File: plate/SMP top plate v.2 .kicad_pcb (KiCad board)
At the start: 2 copper layers, 123.8 x 58.7 mm, 4 parts

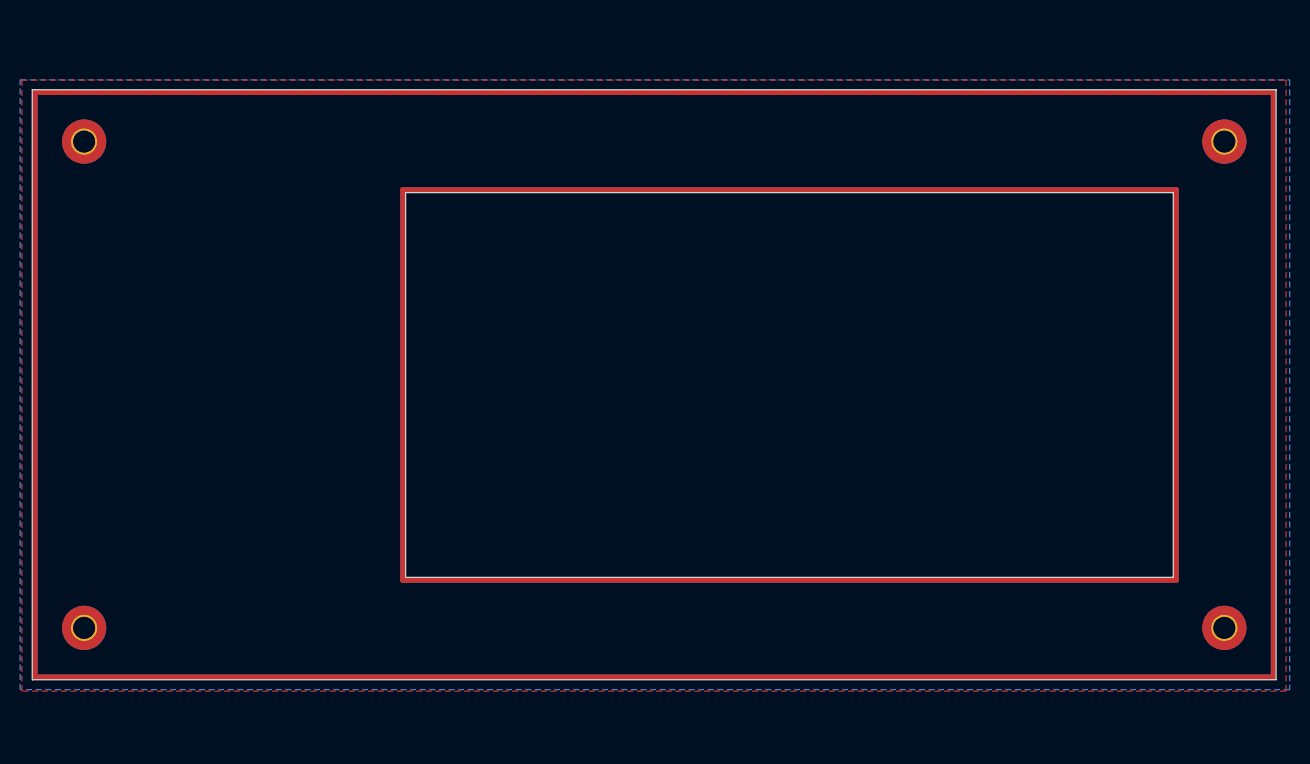
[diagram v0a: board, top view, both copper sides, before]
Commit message: update top plate
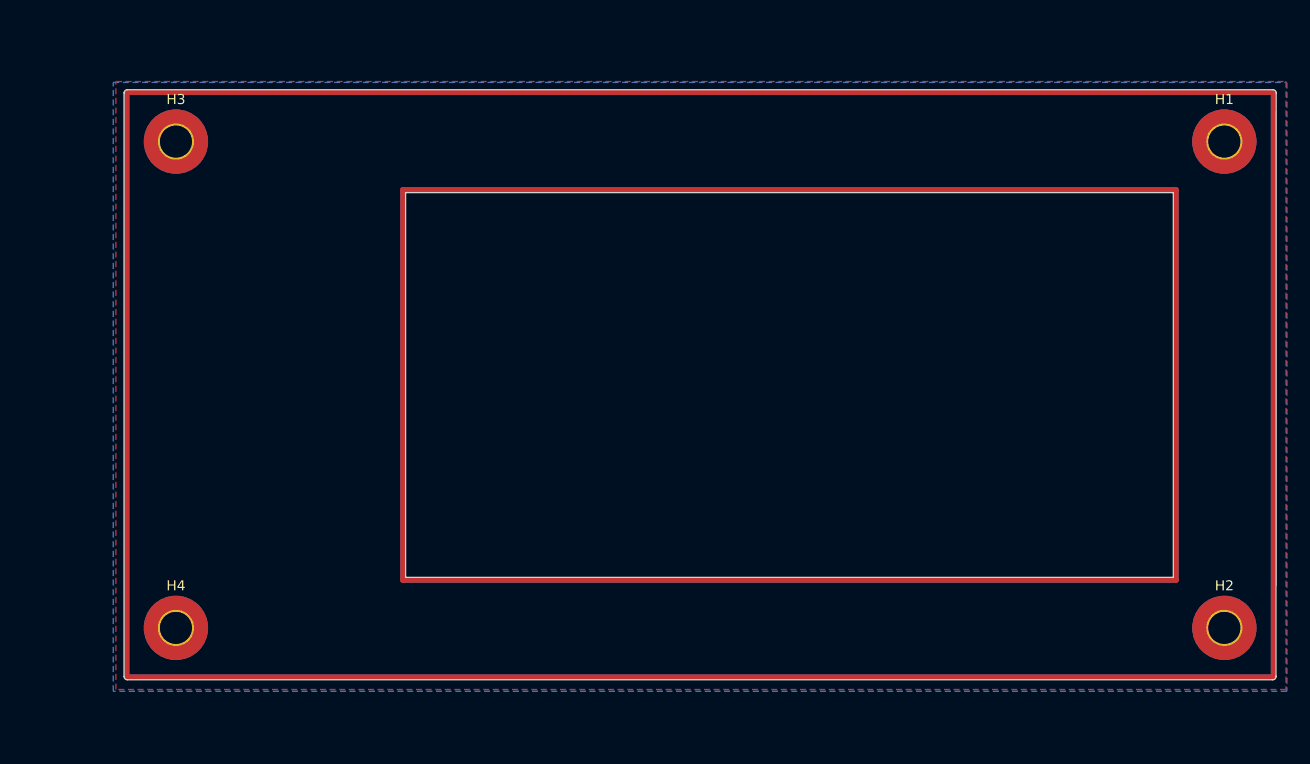
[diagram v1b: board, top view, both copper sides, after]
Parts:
- H1, H2, H3, H4: footprint MountingHole:MountingHole_2.2mm_M2_Pad_TopBottom -> MountingHole:MountingHole_3.2mm_M3_Pad_TopBottom
- moved H1 113.5 mm to (189.1, 76.4)
- moved H2 113.5 mm to (189.1, 124.8)
- moved H3 104.4 mm to (84.7, 76.4)
- moved H4 104.4 mm to (84.7, 124.8)
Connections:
- H1 pad 1: GND -> Net-(H1-Pad1)
- H2 pad 1: GND -> Net-(H2-Pad1)
- H3 pad 1: GND -> Net-(H3-Pad1)
- H4 pad 1: GND -> Net-(H4-Pad1)
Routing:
- added copper zone on B.Cu, net (none)
- added copper zone on F.Cu, net (none)
- removed copper zone on B.Cu, net GND
- removed copper zone on F.Cu, net GND
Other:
- board size 123.8 x 58.7 mm -> 114.7 x 58.7 mm

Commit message: pcb and plate finalize for v.4
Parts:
- added Ref**: Val**, 8hands:urbit-sigil-silks, F.Cu at (106.7, 120.3)
- added kibuzzard-6147B285: G***, label, F.Cu at (106.7, 127.9)
- added kibuzzard-6147B2C4: G***, label, F.Cu at (103.3, 112.6)
- moved H4 97.3 mm to (181.8, 131.5)
- moved H1 94.5 mm to (94.9, 69.0)
- moved H2 56.3 mm to (181.8, 69.0)
- moved H3 56.1 mm to (94.9, 131.5)
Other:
- board size 114.7 x 58.7 mm -> 94.1 x 69.7 mm
- board text added: "The Macropad"
- board text added: "rev.4"

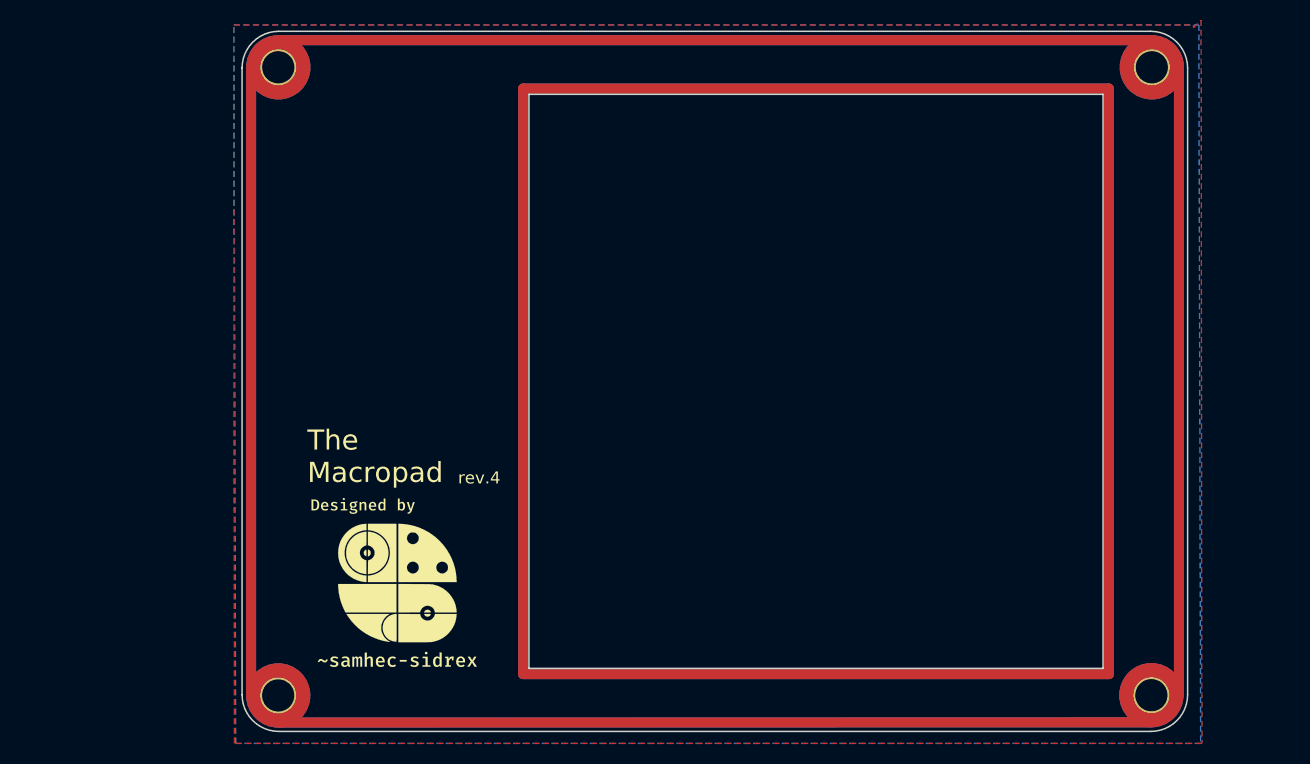
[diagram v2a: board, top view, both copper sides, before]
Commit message: add top plate
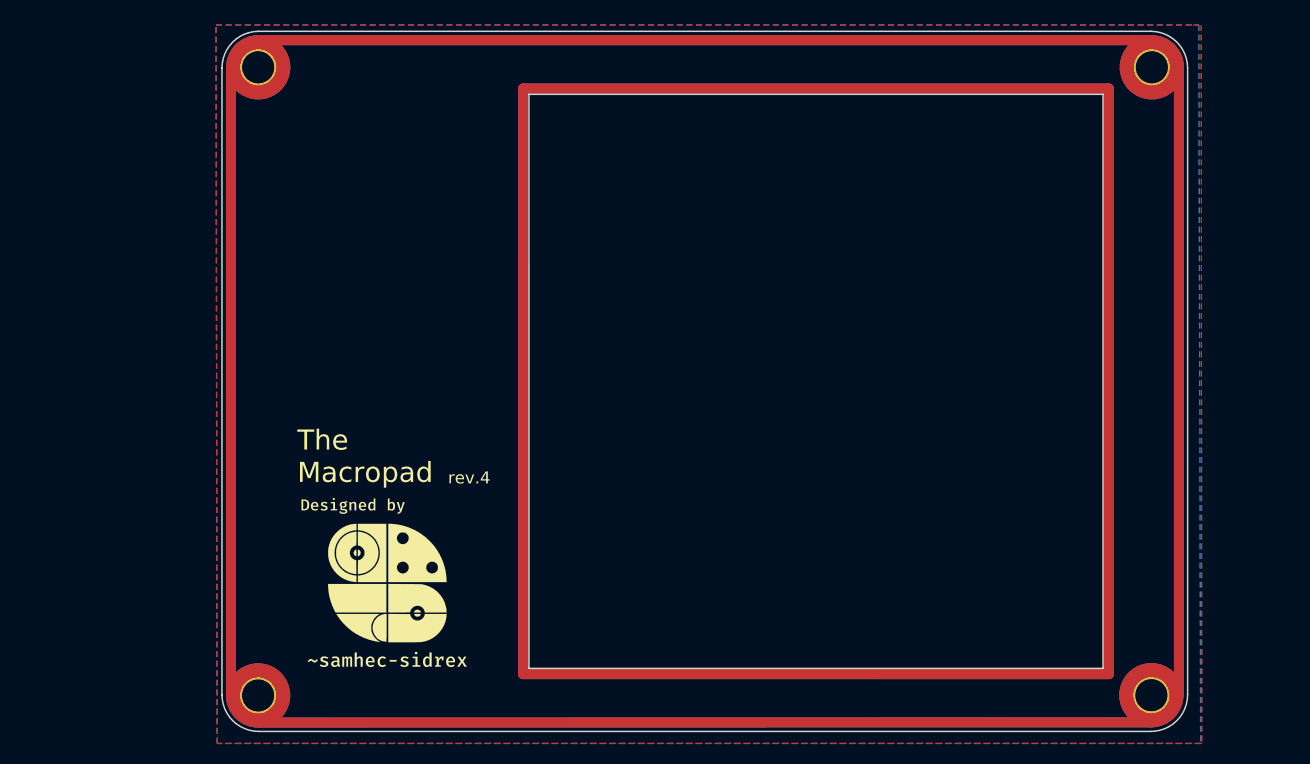
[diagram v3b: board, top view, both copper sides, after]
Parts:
- moved H1 2.00 mm to (92.9, 69.0)
- moved H3 2.00 mm to (92.9, 131.5)
- moved Ref** 1.00 mm to (105.7, 120.3)
- moved kibuzzard-6147B285 1.00 mm to (105.7, 127.9)
- moved kibuzzard-6147B2C4 1.00 mm to (102.3, 112.6)
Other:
- board size 94.1 x 69.7 mm -> 96.1 x 69.7 mm
